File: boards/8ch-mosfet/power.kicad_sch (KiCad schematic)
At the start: 21 parts, among them J3 Screw_Terminal_01x08, J4 Screw_Terminal_01x08, U4 XL1509-5.0

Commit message: updated BOM
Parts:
- C1, C2: Vendor 08053C104KAT4A -> (none)
- C1: LCSC (none) -> C90975; Vendor TAJC107K010RNJ -> (none)
- D18: LCSC (none) -> C908229; Mouser (none) -> 610-CMHSH5-2L; Vendor 610-CMHSH5-2L -> (none)
- D18: Mouser (none) -> 610-CMHSH5-2L; Vendor 610-CMHSH5-2L -> (none)
- D31: LCSC (none) -> C284101
- F10: value mSMD100 -> mSMD110; LCSC (none) -> C69691
- F9: LCSC (none) -> C70113
- FB4: LCSC (none) -> C1017
- J3, J4: now left out of the parts list
- L1: LCSC (none) -> C90321
- L2: LCSC (none) -> C2894721
- R37, R38: Vendor 652-CR0805JW-102ELF -> (none)
- U4: LCSC (none) -> C2902368
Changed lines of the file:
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@@
-      (effects (font (size 1.27 1.27)) hide)
-    )
-    (property "Vendor" "08053C104KAT4A" (at 152.4 87.63 0)
       (effects (font (size 1.27 1.27)) hide)
     )
@@
       (effects (font (size 1.27 1.27)) hide)
     )
-    (property "Vendor" " 610-CMHSH5-2L" (at 195.58 91.44 90)
+    (property "Mouser" " 610-CMHSH5-2L" (at 195.58 91.44 90)
+      (effects (font (size 1.27 1.27)) hide)
+    )
+    (property "LCSC" "C908229" (at 195.58 91.44 90)
       (effects (font (size 1.27 1.27)) hide)
     )
@@
   )
   (symbol (lib_id "Connector:Screw_Terminal_01x08") (at 40.64 144.78 0) (mirror y) (unit 1)
-    (in_bom yes) (on_board yes) (dnp no)
+    (in_bom no) (on_board yes) (dnp no)
     (property "Reference" "J3" (at 40.64 133.35 0)
       (effects (font (size 1.27 1.27)))
@@
       (effects (font (size 1.27 1.27)) hide)
     )
-    (property "Vendor" " 652-CR0805JW-102ELF " (at 166.37 111.76 0)
-      (effects (font (size 1.27 1.27)) hide)
-    )
     (pin "1")
     (pin "2")
@@
       (effects (font (size 1.27 1.27)) hide)
     )
-    (property "Vendor" " 610-CMHSH5-2L" (at 247.65 80.01 90)
+    (property "Mouser" " 610-CMHSH5-2L" (at 247.65 80.01 90)
       (effects (font (size 1.27 1.27)) hide)
     )
@@
   )
   (symbol (lib_id "Connector:Screw_Terminal_01x08") (at 62.23 144.78 0) (mirror y) (unit 1)
-    (in_bom yes) (on_board yes) (dnp no)
+    (in_bom no) (on_board yes) (dnp no)
     (property "Reference" "J4" (at 62.23 133.35 0)
       (effects (font (size 1.27 1.27)))
@@
       (effects (font (size 1.27 1.27)) hide)
     )
+    (property "LCSC" "C2894721" (at 200.66 80.01 90)
+      (effects (font (size 1.27 1.27)) hide)
+    )
     (pin "1")
     (pin "2")
@@
       (effects (font (size 1.27 1.27)) hide)
     )
-    (property "Vendor" "08053C104KAT4A" (at 123.19 87.63 0)
+    (property "Mouser" "" (at 123.19 87.63 0)
       (effects (font (size 1.27 1.27)) hide)
     )
@@
       (effects (font (size 1.27 1.27)) hide)
     )
+    (property "LCSC" "C90321" (at 113.03 80.01 90)
+      (effects (font (size 1.27 1.27)) hide)
+    )
     (pin "1")
     (pin "2")
@@
       (effects (font (size 1.27 1.27)) hide)
     )
-    (property "Vendor" "TAJC107K010RNJ" (at 236.22 87.63 0)
+    (property "LCSC" "C90975" (at 236.22 87.63 0)
       (effects (font (size 1.27 1.27)) hide)
     )
@@
       (effects (font (size 1.27 1.27)) hide)
     )
+    (property "LCSC" "C284101" (at 86.36 87.63 90)
+      (effects (font (size 1.27 1.27)) hide)
+    )
     (pin "1")
     (pin "2")
@@
       (effects (font (size 1.27 1.27)) hide)
     )
+    (property "LCSC" "C1017" (at 60.96 80.01 90)
+      (effects (font (size 1.27 1.27)) hide)
+    )
     (pin "1")
     (pin "2")
@@
     )
     (property "Datasheet" "https://datasheet.lcsc.com/lcsc/1809050422_XLSEMI-XL1509-5-0E1_C61063.pdf" (at 180.34 71.882 0)
+      (effects (font (size 1.27 1.27)) hide)
+    )
+    (property "LCSC" "C2902368" (at 177.8 82.55 0)
       (effects (font (size 1.27 1.27)) hide)
     )
@@
       (effects (font (size 1.27 1.27)) hide)
     )
-    (property "Vendor" "08053C104KAT4A" (at 69.85 87.63 0)
+    (property "Mouser" "" (at 69.85 87.63 0)
       (effects (font (size 1.27 1.27)) hide)
     )
@@
       (effects (font (size 1.27 1.27)) hide)
     )
-    (property "Vendor" "08053C104KAT4A" (at 138.43 83.82 0)
+    (property "Mouser" "" (at 138.43 83.82 0)
       (effects (font (size 1.27 1.27)) hide)
     )
@@
       (effects (font (size 1.27 1.27)))
     )
-    (property "Value" "mSMD100" (at 227.33 76.2 90)
+    (property "Value" "mSMD110" (at 227.33 76.2 90)
       (effects (font (size 1.27 1.27)))
     )
@@
       (effects (font (size 1.27 1.27)) hide)
     )
+    (property "LCSC" "C69691" (at 227.33 80.01 90)
+      (effects (font (size 1.27 1.27)) hide)
+    )
     (pin "1")
     (pin "2")
@@
     )
     (property "Datasheet" "~" (at 138.43 91.44 0)
-      (effects (font (size 1.27 1.27)) hide)
-    )
-    (property "Vendor" " 652-CR0805JW-102ELF " (at 138.43 91.44 0)
       (effects (font (size 1.27 1.27)) hide)
     )
@@
       (effects (font (size 1.27 1.27)) hide)
     )
+    (property "LCSC" "C70113" (at 43.18 80.01 90)
+      (effects (font (size 1.27 1.27)) hide)
+    )
     (pin "1")
     (pin "2")
@@
     )
     (property "Datasheet" "~" (at 187.96 111.76 0)
-      (effects (font (size 1.27 1.27)) hide)
-    )
-    (property "Vendor" " 652-CR0805JW-102ELF " (at 187.96 111.76 0)
       (effects (font (size 1.27 1.27)) hide)
     )
@@
       (effects (font (size 1.27 1.27)) hide)
     )
-    (property "Vendor" " 610-CMHSH5-2L" (at 95.25 80.01 90)
-      (effects (font (size 1.27 1.27)) hide)
-    )
+    (property "Mouser" " 610-CMHSH5-2L" (at 95.25 80.01 90)
+      (effects (font (size 1.27 1.27)) hide)
+    )

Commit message: more BOM updates.
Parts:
- D18: Mouser 610-CMHSH5-2L -> 241-SX33L_R1_00001
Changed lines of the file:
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@@
       (effects (font (size 1.27 1.27)) hide)
     )
-    (property "Mouser" " 610-CMHSH5-2L" (at 247.65 80.01 90)
+    (property "Mouser" " 241-SX33L_R1_00001" (at 247.65 80.01 90)
       (effects (font (size 1.27 1.27)) hide)
     )
@@
       (effects (font (size 1.27 1.27)) hide)
     )
-    (property "Mouser" " 610-CMHSH5-2L" (at 95.25 80.01 90)
-      (effects (font (size 1.27 1.27)) hide)
-    )
+    (property "Mouser" " 241-SX33L_R1_00001" (at 95.25 80.01 90)
+      (effects (font (size 1.27 1.27)) hide)
+    )

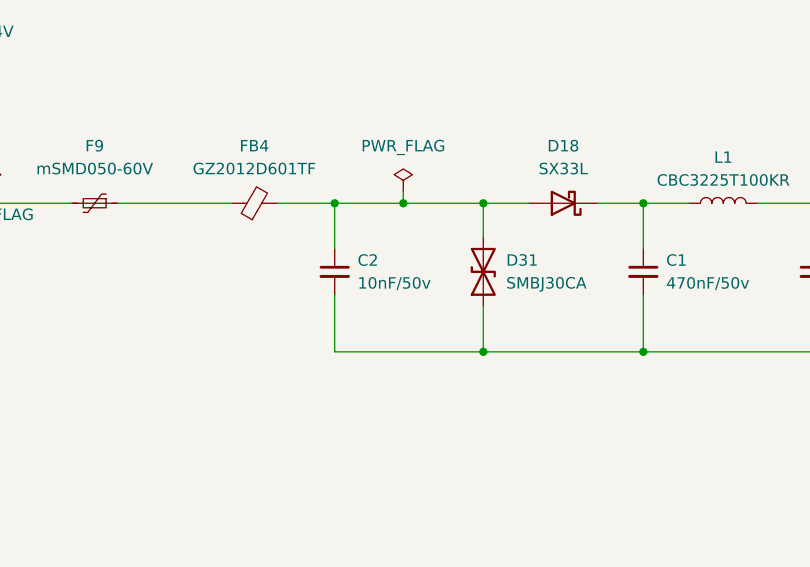
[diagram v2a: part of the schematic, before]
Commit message: oof, working from the wrong copy, had to redo some stuff
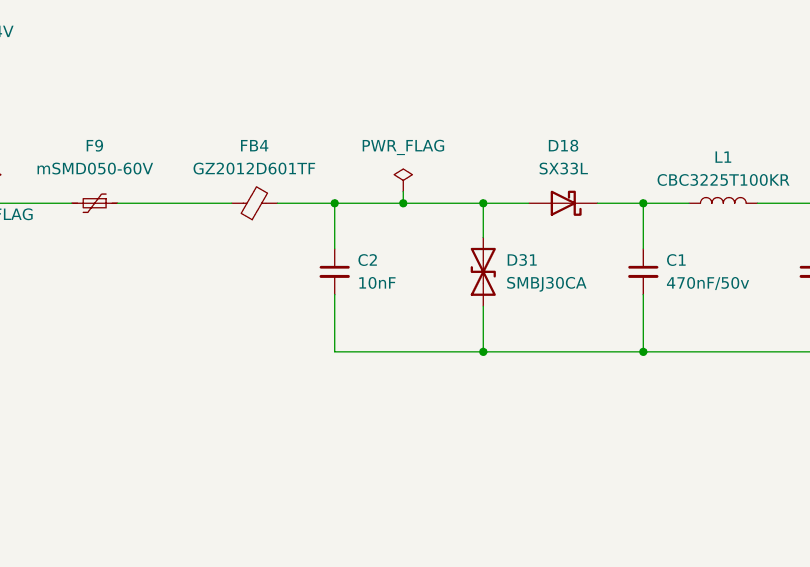
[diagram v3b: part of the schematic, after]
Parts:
- C2: value 10nF/50v -> 10nF
- L2: footprint Inductor_SMD:L_Chilisin_BMRA00040420 -> Inductor_SMD:L_Chilisin_BMRB00060650
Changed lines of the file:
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@@
   (title_block
     (title "Yarrboard 8ch Mosfet Driver")
+    (rev "C1")
     (company "https://github.com/hoeken/yarrboard")
   )
@@
       (effects (font (size 1.27 1.27)))
     )
-    (property "Footprint" "Inductor_SMD:L_Chilisin_BMRA00040420" (at 200.66 80.01 0)
+    (property "Footprint" "Inductor_SMD:L_Chilisin_BMRB00060650" (at 200.66 80.01 0)
       (effects (font (size 1.27 1.27)) hide)
     )
@@
       (effects (font (size 1.27 1.27)) (justify left))
     )
-    (property "Value" "10nF/50v" (at 72.39 88.9063 0)
+    (property "Value" "10nF" (at 72.39 88.9063 0)
       (effects (font (size 1.27 1.27)) (justify left))
     )
